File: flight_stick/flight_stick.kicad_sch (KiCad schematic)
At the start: 71 parts, among them J1 Load Cell 1, J10 USB_C_Receptacle_USB2.0, J11 Conn_01x05_Pin, J3 Load Cell 5, J5 Load Cell 3, J7 Conn_01x04_Male, J8 Conn_01x05_Pin, J9 Conn_ST_STDC14, Q1 MMS8550, Q3 MMS8550, Q4 2N7002, Q5 2N7002, Q6 2N7002, Q7 2N7002, Q8 2N7002, SW1 SW_Push, SW2 SW_Push, U1 HX711, U3 HX711, U4 STM32F103C8Tx, U5 LM3940IMP-3.3/NOPB, Y1 8Mhz

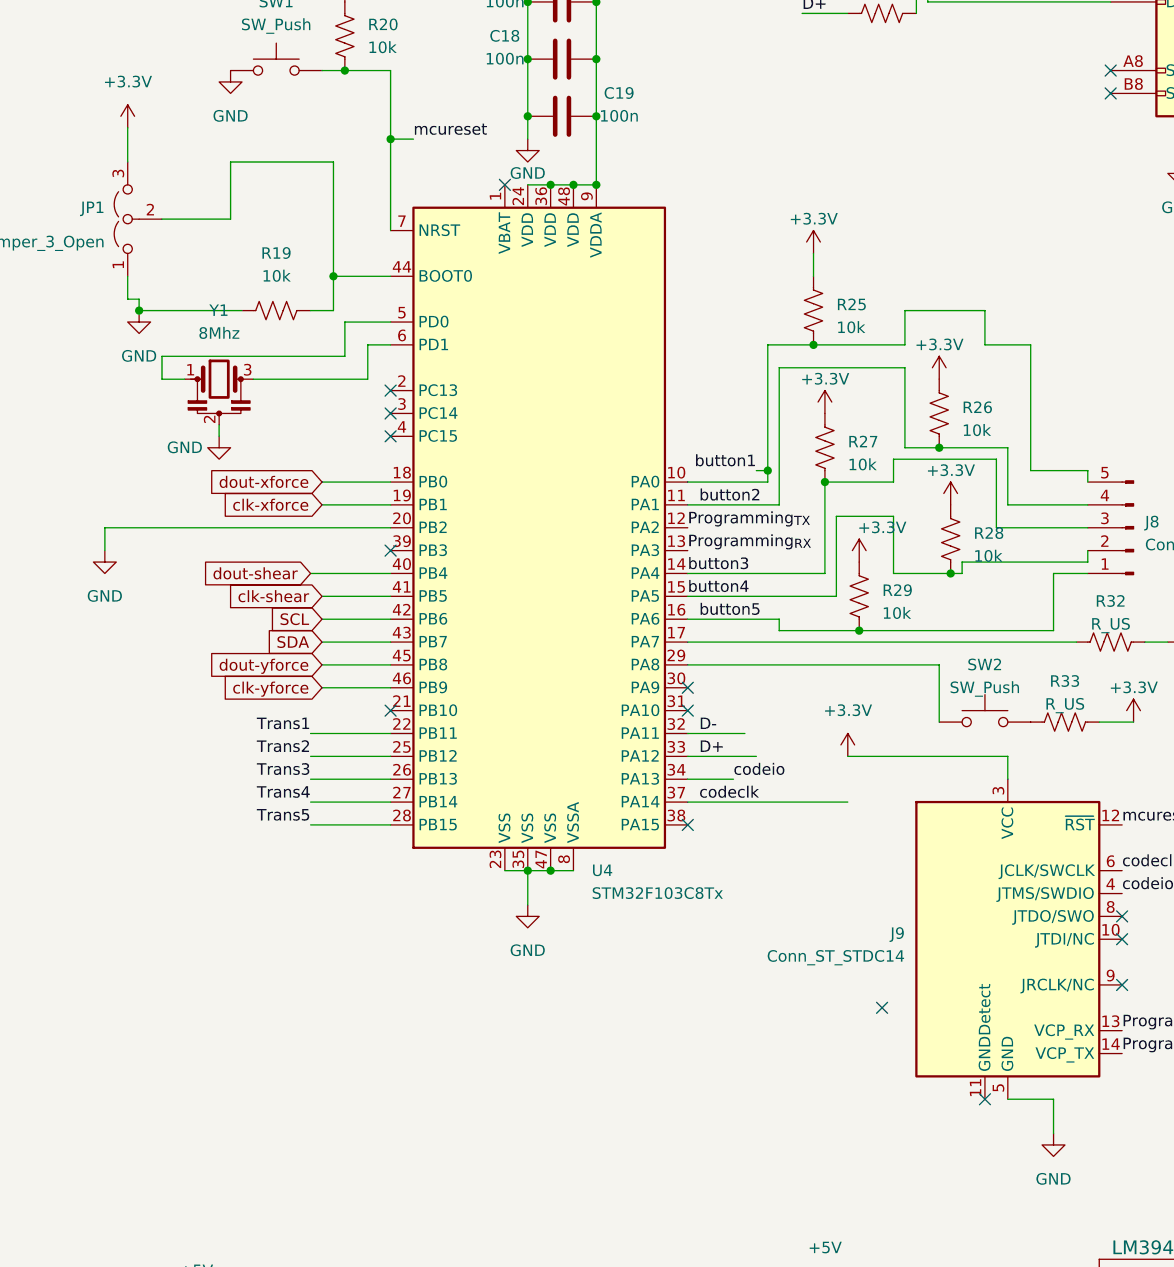
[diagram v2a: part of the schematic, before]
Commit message: updated flight stick schematic
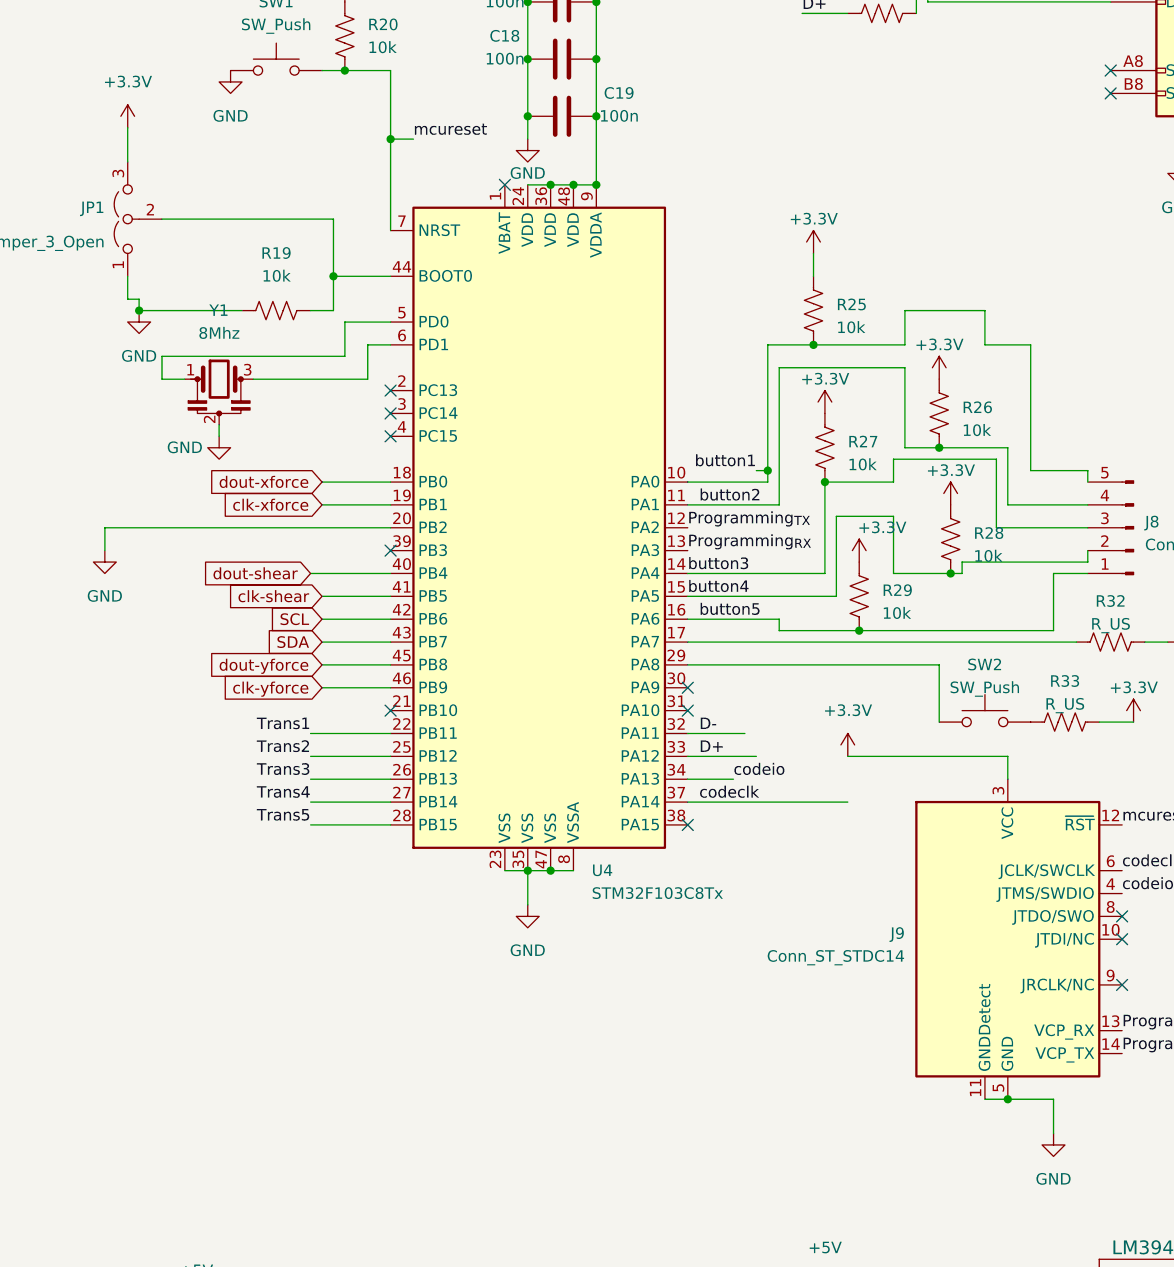
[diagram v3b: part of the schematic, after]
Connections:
- net GND: now also J9.11 (GNDDetect)
- no-connect marks 21 -> 19
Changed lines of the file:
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@@
   (junction (at 325.12 53.34) (diameter 0) (color 0 0 0 0)
+  )
+  (junction (at 317.5 181.61) (diameter 0) (color 0 0 0 0)
   )
   (junction (at 148.59 71.12) (diameter 0) (color 0 0 0 0)
@@
   (no_connect (at 330.2 161.29))
   (no_connect (at 261.62 80.01))
-  (no_connect (at 303.53 171.45))
   (no_connect (at 248.92 107.95))
   (no_connect (at 117.475 141.605))
@@
   (no_connect (at 248.92 120.65))
   (no_connect (at 281.94 138.43))
-  (no_connect (at 314.96 181.61))
   (no_connect (at 248.92 102.87))
   (no_connect (at 117.475 144.145))
@@
     (stroke (width 0) (type default))
   )
-  (wire (pts (xy 242.57 77.47) (xy 242.57 90.17))
+  (wire (pts (xy 242.57 83.82) (xy 242.57 90.17))
     (stroke (width 0) (type default))
   )
@@
     (stroke (width 0) (type default))
   )
-  (wire (pts (xy 242.57 77.47) (xy 231.14 77.47))
-    (stroke (width 0) (type default))
-  )
   (wire (pts (xy 298.45 125.73) (xy 281.94 125.73))
     (stroke (width 0) (type default))
@@
     (stroke (width 0) (type default))
   )
-  (wire (pts (xy 231.14 83.82) (xy 223.52 83.82))
+  (wire (pts (xy 223.52 83.82) (xy 242.57 83.82))
     (stroke (width 0) (type default))
   )
@@
     (stroke (width 0) (type default))
   )
+  (wire (pts (xy 317.5 181.61) (xy 322.58 181.61))
+    (stroke (width 0) (type default))
+  )
   (wire (pts (xy 344.17 77.47) (xy 336.55 77.47))
     (stroke (width 0) (type default))
@@
     (stroke (width 0) (type default))
   )
-  (wire (pts (xy 231.14 77.47) (xy 231.14 83.82))
-    (stroke (width 0) (type default))
-  )
   (wire (pts (xy 308.61 59.69) (xy 308.61 58.42))
     (stroke (width 0) (type default))
@@
     (stroke (width 0) (type default))
   )
-  (wire (pts (xy 317.5 181.61) (xy 322.58 181.61))
-    (stroke (width 0) (type default))
-  )
+  (wire (pts (xy 314.96 181.61) (xy 317.5 181.61))
+    (stroke (width 0) (type default))
+  )

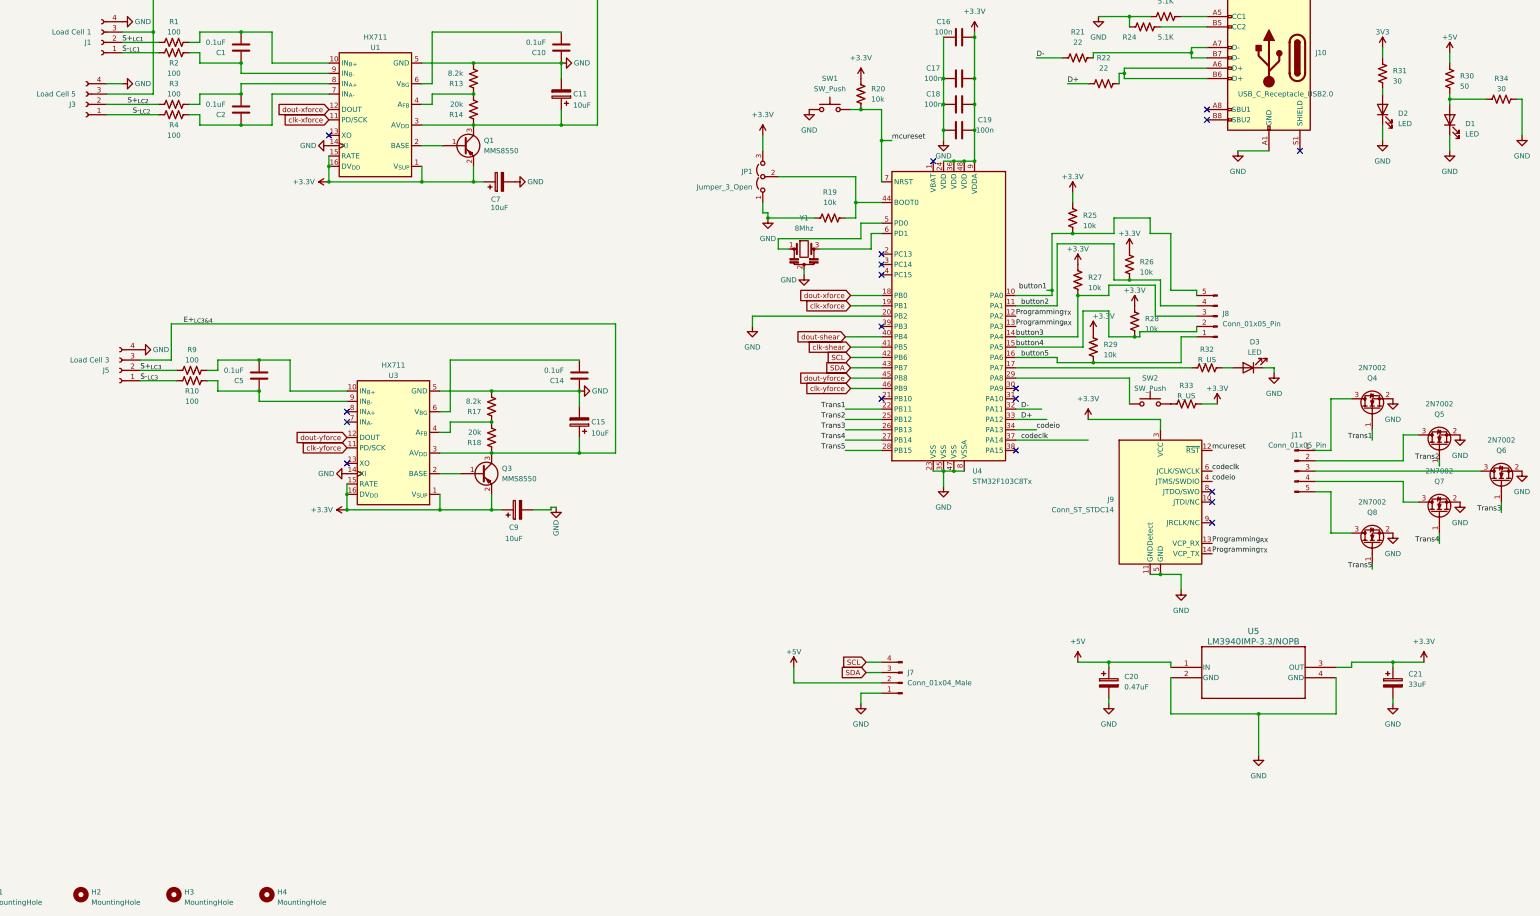
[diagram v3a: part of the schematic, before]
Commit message: Made Recommended changes
From savo:
C11 is a decoupling capacitor for one of the HX711s, it should be closer to it
You can get rid of two of the mounting holes. Two are enough.
Try to bring the USB stuff closer to the STM32, since it operates at high speed and we should keep the connections short.
Similarly try to bring the programming header closer to the STM32.
You can move the button stuff further from the STM32, those will be operated at kHz which is "slow"
The resistors you picked for the LEDs are a fair bit smaller than needed, 100+ Ohms is good.
No need for the pulldown R34
Power LEDs are cool, but maybe just one on the 3V3 rail is enough since thats the critical line. You can probably use the other one as a user configurable one too
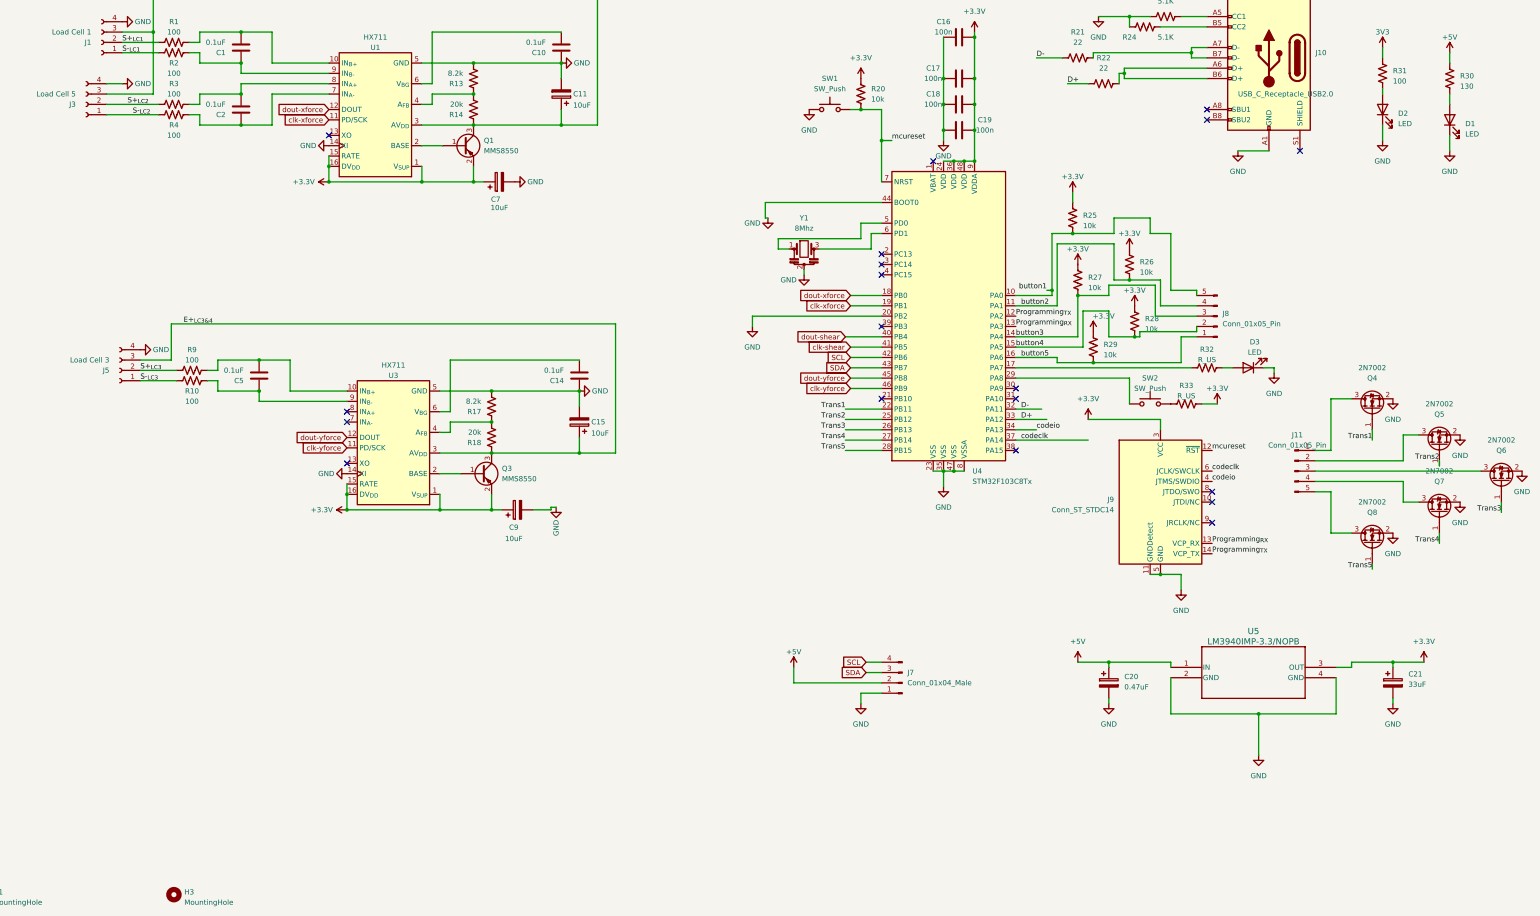
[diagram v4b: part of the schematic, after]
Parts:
- removed H2, H4: MountingHole, MountingHole:MountingHole_3.2mm_M3_ISO7380, symbol Mechanical:MountingHole
- removed JP1: Jumper_3_Open, Jumper:SolderJumper-3_P2.0mm_Open_TrianglePad1.0x1.5mm, symbol Jumper:Jumper_3_Open
- removed R19: 10k, Resistor_SMD:R_0603_1608Metric, symbol Device:R_US
- removed R34: 30, Resistor_SMD:R_0603_1608Metric, symbol Device:R_US
- R30: value 50 -> 130
- R31: value 30 -> 100
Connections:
- net GND: now also U4.44 (BOOT0)

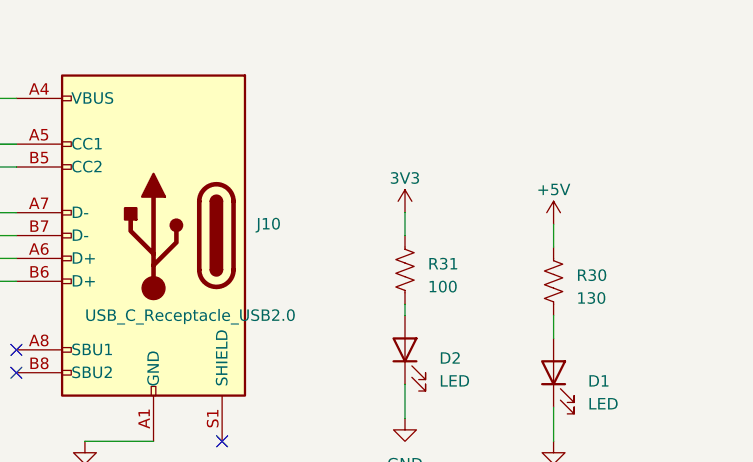
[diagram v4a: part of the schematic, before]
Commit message: Updated Layout
Board is now symetrical and necessary components are locked
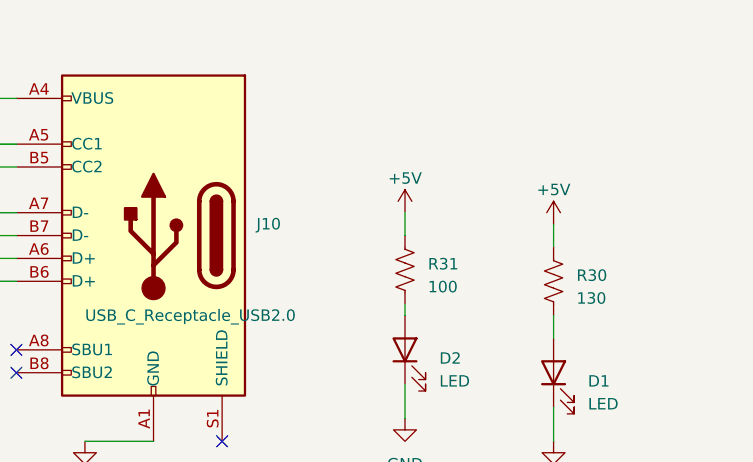
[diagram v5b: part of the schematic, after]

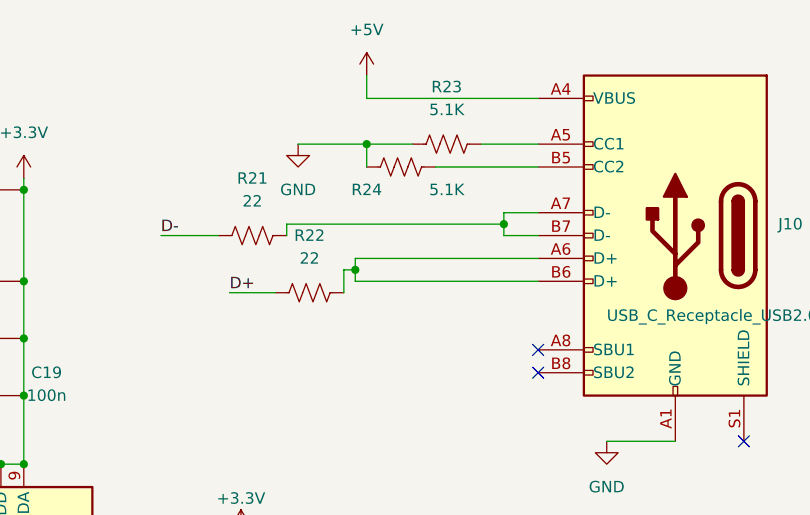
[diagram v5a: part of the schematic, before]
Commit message: Finalilzed Layout and began routing
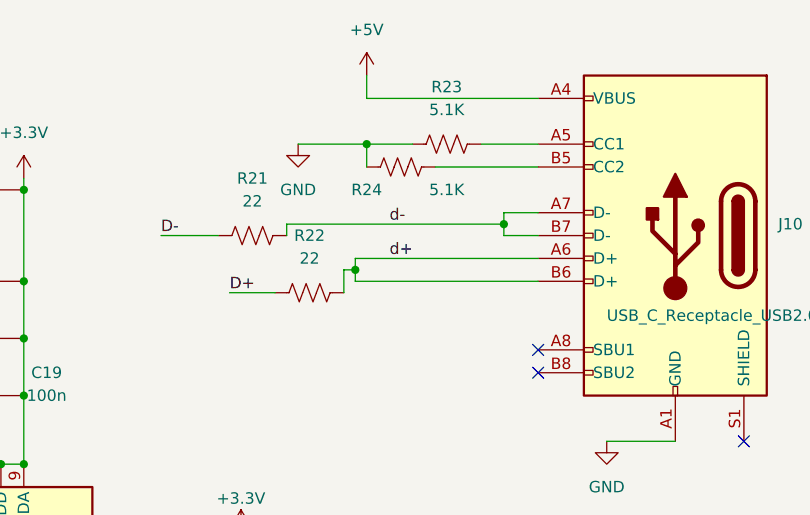
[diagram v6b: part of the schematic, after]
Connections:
- net d-: now reaches J10.A7 (D-), J10.B7 (D-), R21.2
- net d+: now reaches J10.A6 (D+), J10.B6 (D+), R22.2
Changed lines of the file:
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@@
+		)
+	)
+	(label "d+"
+		(at 312.42 57.15 0)
+		(fields_autoplaced yes)
+		(effects
+			(font
+				(size 1.27 1.27)
+			)
+			(justify left bottom)
 		)
 	)
@@
 		(fields_autoplaced yes)
 		(effects
+			(font
+				(size 1.27 1.27)
+			)
+			(justify left bottom)
+		)
+	)
+	(label "d-"
+		(at 312.42 53.34 0)
+		(fields_autoplaced yes)
+		(effects
